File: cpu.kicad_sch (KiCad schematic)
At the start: 33 parts, among them IC12 DS2401+, IC13 ARM250, IC20 74HC138, IC27 74AC32, IC8 74HCT14, X4 72.0MHz, X5 25.175MHz

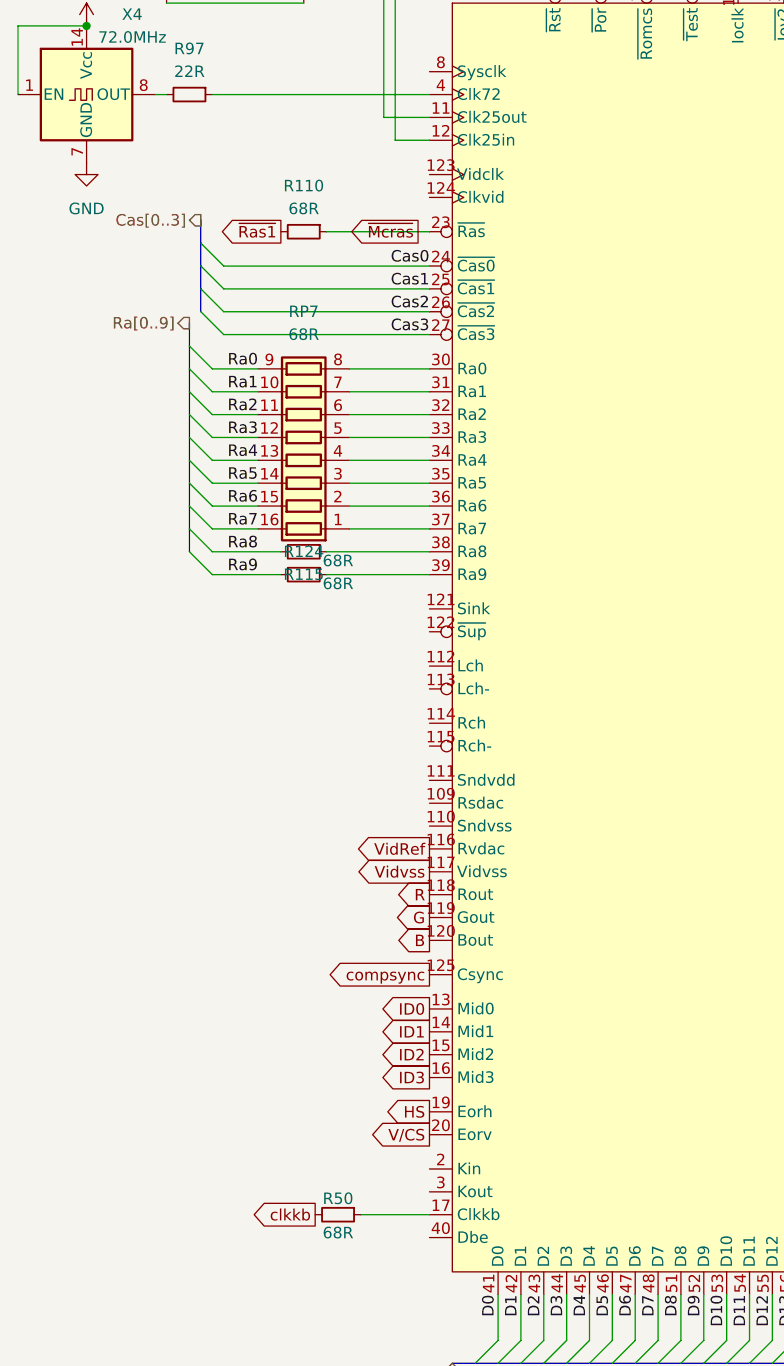
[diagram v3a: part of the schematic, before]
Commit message: add rf video output
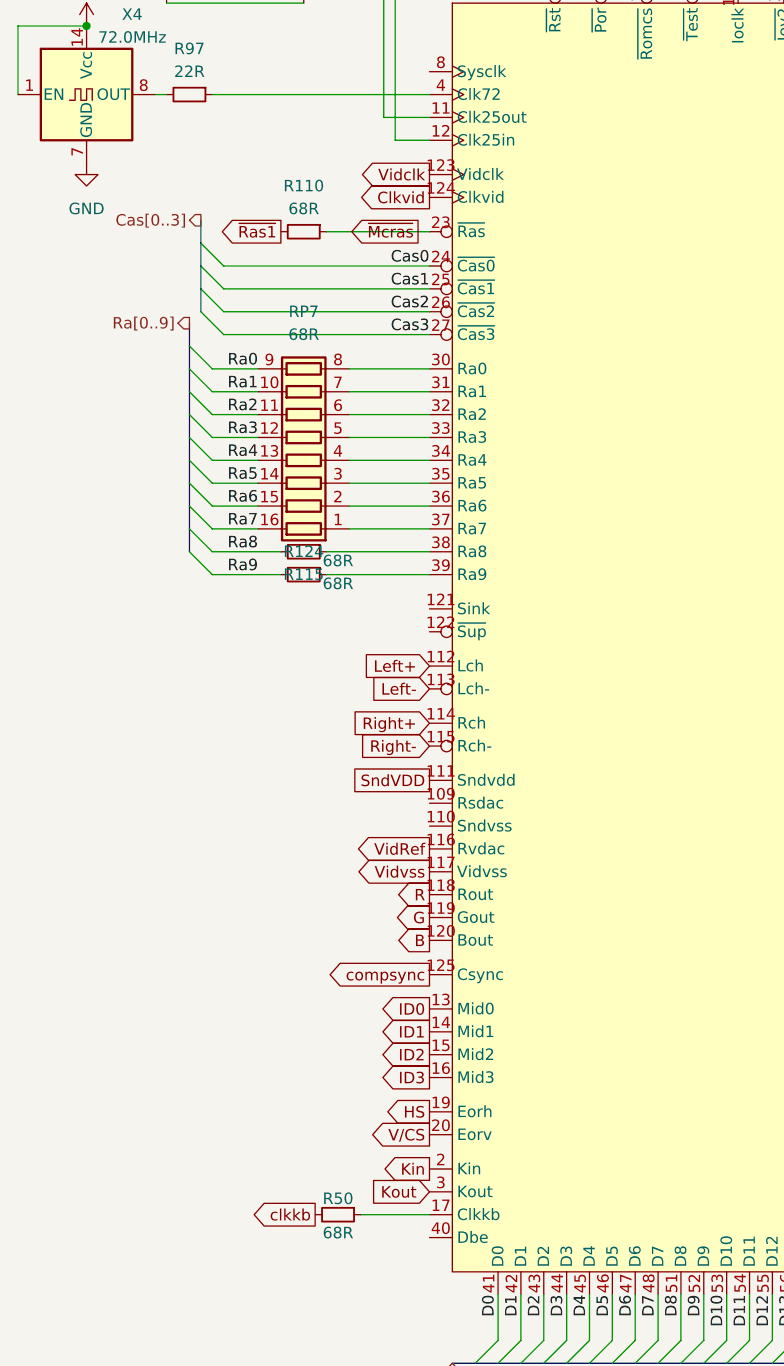
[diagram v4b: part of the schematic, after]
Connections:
- net SndVDD: now reaches IC13.111 (Sndvdd)
- net Left+: now reaches IC13.112 (Lch)
- net Left-: now reaches IC13.113 (Lch-)
- net Right+: now reaches IC13.114 (Rch)
- net Right-: now reaches IC13.115 (Rch-)
- net Vidclk: now reaches IC13.123 (Vidclk)
- net Clkvid: now reaches IC13.124 (Clkvid)
- net Kin: now reaches IC13.2 (Kin)
- net Kout: now reaches IC13.3 (Kout)
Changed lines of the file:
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@@
+		)
+	)
+	(global_label "Left-"
+		(shape input)
+		(at 92.71 165.1 180)
+		(fields_autoplaced yes)
+		(effects
+			(font
+				(size 1.27 1.27)
+			)
+			(justify right)
+		)
+		(property "Intersheetrefs" "${INTERSHEET_REFS}"
+			(at 84.5843 165.1 0)
+			(effects
+				(font
+					(size 1.27 1.27)
+				)
+				(justify right)
+				(hide yes)
+			)
 		)
 	)
@@
 		)
 	)
+	(global_label "Right+"
+		(shape input)
+		(at 92.71 168.91 180)
+		(fields_autoplaced yes)
+		(effects
+			(font
+				(size 1.27 1.27)
+			)
+			(justify right)
+		)
+		(property "Intersheetrefs" "${INTERSHEET_REFS}"
+			(at 83.2539 168.91 0)
+			(effects
+				(font
+					(size 1.27 1.27)
+				)
+				(justify right)
+				(hide yes)
+			)
+		)
+	)
 	(global_label "ID2"
 		(shape output)
@@
 		)
 	)
+	(global_label "Right-"
+		(shape input)
+		(at 92.71 171.45 180)
+		(fields_autoplaced yes)
+		(effects
+			(font
+				(size 1.27 1.27)
+			)
+			(justify right)
+		)
+		(property "Intersheetrefs" "${INTERSHEET_REFS}"
+			(at 83.2539 171.45 0)
+			(effects
+				(font
+					(size 1.27 1.27)
+				)
+				(justify right)
+				(hide yes)
+			)
+		)
+	)
 	(global_label "G"
 		(shape output)
@@
 		)
 	)
+	(global_label "Vidclk"
+		(shape output)
+		(at 92.71 107.95 180)
+		(fields_autoplaced yes)
+		(effects
+			(font
+				(size 1.27 1.27)
+			)
+			(justify right)
+		)
+		(property "Intersheetrefs" "${INTERSHEET_REFS}"
+			(at 84.1005 107.95 0)
+			(effects
+				(font
+					(size 1.27 1.27)
+				)
+				(justify right)
+				(hide yes)
+			)
+		)
+	)
 	(global_label "~{Ps1}"
 		(shape output)
@@
 		)
 	)
+	(global_label "Left+"
+		(shape input)
+		(at 92.71 162.56 180)
+		(fields_autoplaced yes)
+		(effects
+			(font
+				(size 1.27 1.27)
+			)
+			(justify right)
+		)
+		(property "Intersheetrefs" "${INTERSHEET_REFS}"
+			(at 84.5843 162.56 0)
+			(effects
+				(font
+					(size 1.27 1.27)
+				)
+				(justify right)
+				(hide yes)
+			)
+		)
+	)
+	(global_label "Clkvid"
+		(shape output)
+		(at 92.71 110.49 180)
+		(fields_autoplaced yes)
+		(effects
+			(font
+				(size 1.27 1.27)
+			)
+			(justify right)
+		)
+		(property "Intersheetrefs" "${INTERSHEET_REFS}"
+			(at 84.0401 110.49 0)
+			(effects
+				(font
+					(size 1.27 1.27)
+				)
+				(justify right)
+				(hide yes)
+			)
+		)
+	)
 	(global_label "~{Romcs}"
 		(shape input)
@@
 		)
 	)
+	(global_label "Kout"
+		(shape input)
+		(at 92.71 220.98 180)
+		(fields_autoplaced yes)
+		(effects
+			(font
+				(size 1.27 1.27)
+			)
+			(justify right)
+		)
+		(property "Intersheetrefs" "${INTERSHEET_REFS}"
+			(at 85.4311 220.98 0)
+			(effects
+				(font
+					(size 1.27 1.27)
+				)
+				(justify right)
+				(hide yes)
+			)
+		)
+	)
 	(global_label "~{Joyst1}"
 		(shape output)
@@
 		)
 	)
+	(global_label "SndVDD"
+		(shape passive)
+		(at 92.71 175.26 180)
+		(fields_autoplaced yes)
+		(effects
+			(font
+				(size 1.27 1.27)
+			)
+			(justify right)
+		)
+		(property "Intersheetrefs" "${INTERSHEET_REFS}"
+			(at 83.7 175.26 0)
+			(effects
+				(font
+					(size 1.27 1.27)
+				)
+				(justify right)
+				(hide yes)
+			)
+		)
+	)
 	(global_label "VidRef"
 		(shape output)
@@
 			(effects
 				(font
+					(size 1.27 1.27)
+				)
+				(justify right)
+				(hide yes)
+			)
+		)
+	)
+	(global_label "Kin"
+		(shape output)
+		(at 92.71 218.44 180)
+		(fields_autoplaced yes)
+		(effects
+			(font
+				(size 1.27 1.27)
+			)
+			(justify right)
+		)
+		(property "Intersheetrefs" "${INTERSHEET_REFS}"
+			(at 86.701 218.44 0)
+			(effects
+				(font

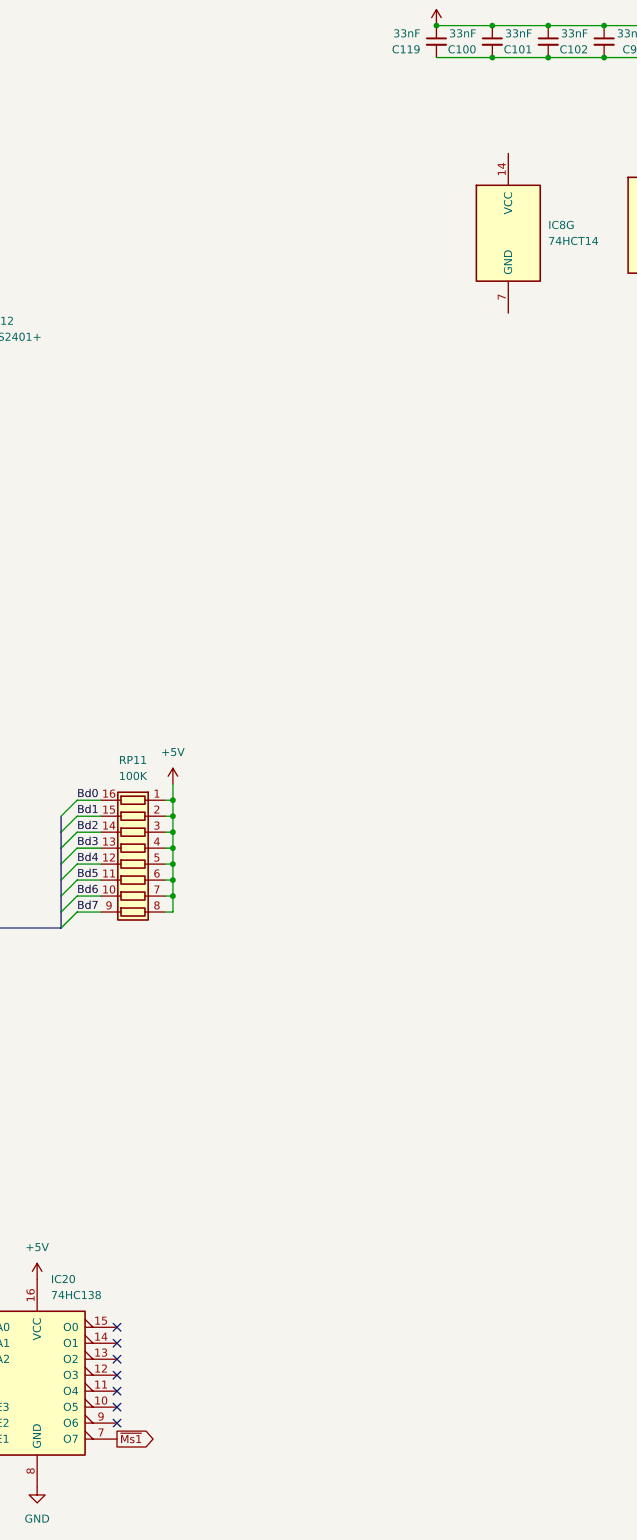
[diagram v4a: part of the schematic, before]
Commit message: wire in LA bus
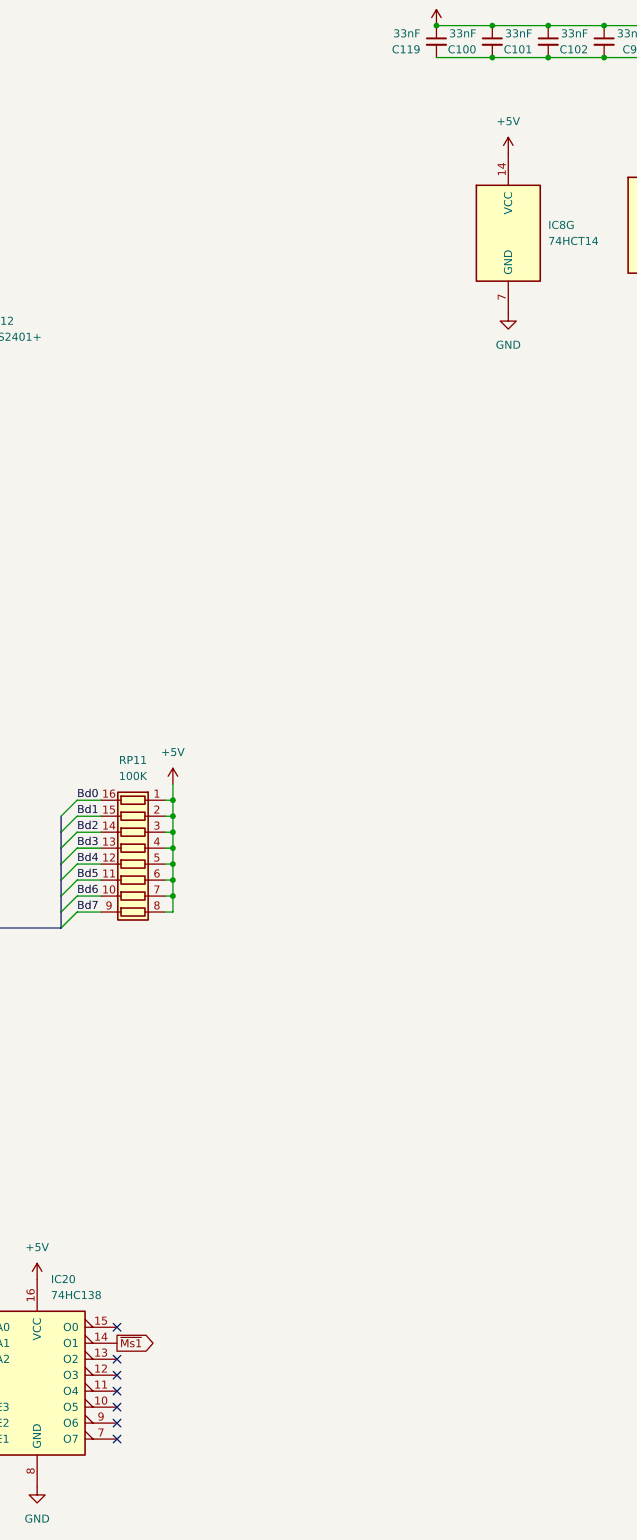
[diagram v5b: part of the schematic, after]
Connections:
- net +5V: now also IC8.14 (VCC)
- net GND: now also IC8.7 (GND)
- net ~{Ms1}: now also IC20.14 (O1); no longer IC20.7 (O7)
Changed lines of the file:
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@@
 	)
 	(no_connect
-		(at 260.35 240.03)
-	)
-	(no_connect
 		(at 260.35 237.49)
 	)
@@
 	)
 	(no_connect
+		(at 260.35 255.27)
+	)
+	(no_connect
 		(at 260.35 247.65)
 	)
@@
 		)
 	)
+	(global_label "~{Ms1}"
+		(shape output)
+		(at 260.35 240.03 0)
+		(fields_autoplaced yes)
+		(effects
+			(font
+				(size 1.27 1.27)
+			)
+			(justify left)
+		)
+		(property "Intersheetrefs" "${INTERSHEET_REFS}"
+			(at 267.0242 240.03 0)
+			(effects
+				(font
+					(size 1.27 1.27)
+				)
+				(justify left)
+				(hide yes)
+			)
+		)
+	)
 	(global_label "C0"
 		(shape input)
@@
 		)
 	)
-	(global_label "~{Ms1}"
-		(shape output)
-		(at 260.35 255.27 0)
-		(fields_autoplaced yes)
-		(effects
-			(font
-				(size 1.27 1.27)
-			)
-			(justify left)
-		)
-		(property "Intersheetrefs" "${INTERSHEET_REFS}"
-			(at 267.0242 255.27 0)
-			(effects
-				(font
-					(size 1.27 1.27)
-				)
-				(justify left)
-				(hide yes)
-			)
-		)
-	)
 	(global_label "~{Bl}"
 		(shape input)
@@
 	)
 	(symbol
+		(lib_id "power:GND")
+		(at 322.58 76.2 0)
+		(unit 1)
+		(exclude_from_sim no)
+		(in_bom yes)
+		(on_board yes)
+		(dnp no)
+		(fields_autoplaced yes)
+		(property "Reference" "#PWR0284"
+			(at 322.58 82.55 0)
+			(effects
+				(font
+					(size 1.27 1.27)
+				)
+				(hide yes)
+			)
+		)
+		(property "Value" "GND"
+			(at 322.58 81.28 0)
+			(effects
+				(font
+					(size 1.27 1.27)
+				)
+			)
+		)
+		(property "Footprint" ""
+			(at 322.58 76.2 0)
+			(effects
+				(font
+					(size 1.27 1.27)
+				)
+				(hide yes)
+			)
+		)
+		(property "Datasheet" ""
+			(at 322.58 76.2 0)
+			(effects
+				(font
+					(size 1.27 1.27)
+				)
+				(hide yes)
+			)
+		)
+		(property "Description" "Power symbol creates a global label with name \"GND\" , ground"
+			(at 322.58 76.2 0)
+			(effects
+				(font
+					(size 1.27 1.27)
+				)
+				(hide yes)
+			)
+		)
+		(pin "1"
+		)
+		(instances
+			(project "Acorn-A3010"
+				(path "/999882f3-94f8-4a89-9093-27a47d0cb289/5f74aac3-9761-4bed-8486-119acb837e61"
+					(reference "#PWR0284")
+					(unit 1)
+				)
+			)
+		)
+	)
+	(symbol
 		(lib_id "power:+5V")
 		(at 228.6 250.19 0)
@@
 					(unit 1)
 				)
+			)
+		)
+	)
+	(symbol
+		(lib_id "power:+5V")
+		(at 322.58 50.8 0)
+		(unit 1)
+		(exclude_from_sim no)
+		(in_bom yes)
+		(on_board yes)
+		(dnp no)
+		(fields_autoplaced yes)
+		(property "Reference" "#PWR0283"
+			(at 322.58 54.61 0)
+			(effects
+				(font
+					(size 1.27 1.27)
+				)
+				(hide yes)
+			)
+		)
+		(property "Value" "+5V"
+			(at 322.58 45.72 0)
+			(effects
+				(font
+					(size 1.27 1.27)
+				)
+			)
+		)
+		(property "Footprint" ""
+			(at 322.58 50.8 0)
+			(effects
+				(font
+					(size 1.27 1.27)
+				)
+				(hide yes)
+			)
+		)
+		(property "Datasheet" ""
+			(at 322.58 50.8 0)
+			(effects
+				(font
+					(size 1.27 1.27)
+				)
+				(hide yes)
+			)
+		)
+		(property "Description" "Power symbol creates a global label with name \"+5V\""
+			(at 322.58 50.8 0)
+			(effects
+				(font
+					(size 1.27 1.27)
+				)
+				(hide yes)
+			)
+		)
+		(pin "1"
+		)
+		(instances
+			(project "Acorn-A3010"
+				(path "/999882f3-94f8-4a89-9093-27a47d0cb289/5f74aac3-9761-4bed-8486-119acb837e61"
+					(reference "#PWR0283")
+					(unit 1)
+				)

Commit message: tracing refinement
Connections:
- net Dbe: now reaches IC13.40 (Dbe)
- net ~{Ras1} renamed ~{Ras}
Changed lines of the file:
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@@
 		)
 	)
-	(global_label "~{Ras1}"
+	(global_label "Dbe"
+		(shape output)
+		(at 92.71 226.06 180)
+		(fields_autoplaced yes)
+		(effects
+			(font
+				(size 1.27 1.27)
+			)
+			(justify right)
+		)
+		(property "Intersheetrefs" "${INTERSHEET_REFS}"
+			(at 86.2172 226.06 0)
+			(effects
+				(font
+					(size 1.27 1.27)
+				)
+				(justify right)
+				(hide yes)
+			)
+		)
+	)
+	(global_label "~{Ras}"
 		(shape output)
 		(at 76.2 114.3 180)
@@
 		)
 		(property "Intersheetrefs" "${INTERSHEET_REFS}"
-			(at 68.5582 114.3 0)
+			(at 69.7677 114.3 0)
 			(effects
 				(font

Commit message: fix rp11
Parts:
- RP11: value 100K -> 68R
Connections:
- net +5V: no longer RP11.1 (R1.1), RP11.2 (R2.1), RP11.3 (R3.1), RP11.4 (R4.1), RP11.5 (R5.1), RP11.6 (R6.1), RP11.7 (R7.1), RP11.8 (R8.1)
- net Bd0: now also RP11.1 (R1.1); no longer IC13.148 (Bd0), RP11.16 (R1.2)
- net Bd1: now also RP11.2 (R2.1); no longer IC13.149 (Bd1), RP11.15 (R2.2)
- net Bd2: now also RP11.3 (R3.1); no longer IC13.150 (Bd2), RP11.14 (R3.2)
- net Bd3: now also RP11.4 (R4.1); no longer IC13.151 (Bd3), RP11.13 (R4.2)
- net Bd4: now also RP11.5 (R5.1); no longer IC13.152 (Bd4), RP11.12 (R5.2)
- net Bd5: now also RP11.6 (R6.1); no longer IC13.153 (Bd5), RP11.11 (R6.2)
- net Bd6: now also RP11.7 (R7.1); no longer IC13.154 (Bd6), RP11.10 (R7.2)
- net Bd7: now also RP11.8 (R8.1); no longer IC13.155 (Bd7), RP11.9 (R8.2)
- new net: IC13.154 (Bd6), RP11.10 (R7.2)
- new net: IC13.153 (Bd5), RP11.11 (R6.2)
- new net: IC13.152 (Bd4), RP11.12 (R5.2)
- new net: IC13.151 (Bd3), RP11.13 (R4.2)
- new net: IC13.150 (Bd2), RP11.14 (R3.2)
- new net: IC13.149 (Bd1), RP11.15 (R2.2)
- new net: IC13.148 (Bd0), RP11.16 (R1.2)
- new net: IC13.155 (Bd7), RP11.9 (R8.2)
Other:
- moved on the sheet: RP11

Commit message: more traces
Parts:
- RP11: value 68R -> 100K
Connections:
- net +5V: now also RP11.1 (R1.1), RP11.2 (R2.1), RP11.3 (R3.1), RP11.4 (R4.1), RP11.5 (R5.1), RP11.6 (R6.1), RP11.7 (R7.1), RP11.8 (R8.1)
- net Bd0: now also IC13.148 (Bd0), RP11.16 (R1.2); no longer RP11.1 (R1.1)
- net Bd1: now also IC13.149 (Bd1), RP11.15 (R2.2); no longer RP11.2 (R2.1)
- net Bd2: now also IC13.150 (Bd2), RP11.14 (R3.2); no longer RP11.3 (R3.1)
- net Bd3: now also IC13.151 (Bd3), RP11.13 (R4.2); no longer RP11.4 (R4.1)
- net Bd4: now also IC13.152 (Bd4), RP11.12 (R5.2); no longer RP11.5 (R5.1)
- net Bd5: now also IC13.153 (Bd5), RP11.11 (R6.2); no longer RP11.6 (R6.1)
- net Bd6: now also IC13.154 (Bd6), RP11.10 (R7.2); no longer RP11.7 (R7.1)
- net Bd7: now also IC13.155 (Bd7), RP11.9 (R8.2); no longer RP11.8 (R8.1)
- net La17: now also IC20.4 (E1); no longer IC20.5 (E2)
- net La21: now also IC20.5 (E2); no longer IC20.4 (E1)
- net SndRef: now reaches IC13.109 (Rsdac)
- net SndVSS: now reaches IC13.110 (Sndvss)
- net sink: now reaches IC13.121 (Sink)
- net ~{Sup}: now reaches IC13.122 (~{Sup})
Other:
- moved on the sheet: RP11
